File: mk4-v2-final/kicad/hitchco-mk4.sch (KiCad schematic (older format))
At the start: 24 parts, among them J1 Screw_Terminal_01x16, J10 Conn_02x03_Counter_Clockwise, J11 Conn_02x03_Counter_Clockwise, J12 Conn_02x03_Counter_Clockwise, J13 Screw_Terminal_01x16, J14 Conn_02x03_Counter_Clockwise, J15 Conn_02x03_Counter_Clockwise, J16 Conn_02x03_Counter_Clockwise, J17 Conn_02x03_Counter_Clockwise, J18 Conn_02x03_Counter_Clockwise, J19 Conn_02x03_Counter_Clockwise, J2 Conn_02x03_Counter_Clockwise, J20 Conn_02x03_Counter_Clockwise, J21 Conn_02x03_Counter_Clockwise, J22 Conn_02x03_Counter_Clockwise, J23 Conn_02x03_Counter_Clockwise, J24 Conn_02x03_Counter_Clockwise, J3 Conn_02x03_Counter_Clockwise, J4 Screw_Terminal_01x16, J5 Conn_02x03_Counter_Clockwise, J6 Conn_02x03_Counter_Clockwise, J7 Conn_02x03_Counter_Clockwise, J8 Screw_Terminal_01x16, J9 Conn_02x03_Counter_Clockwise

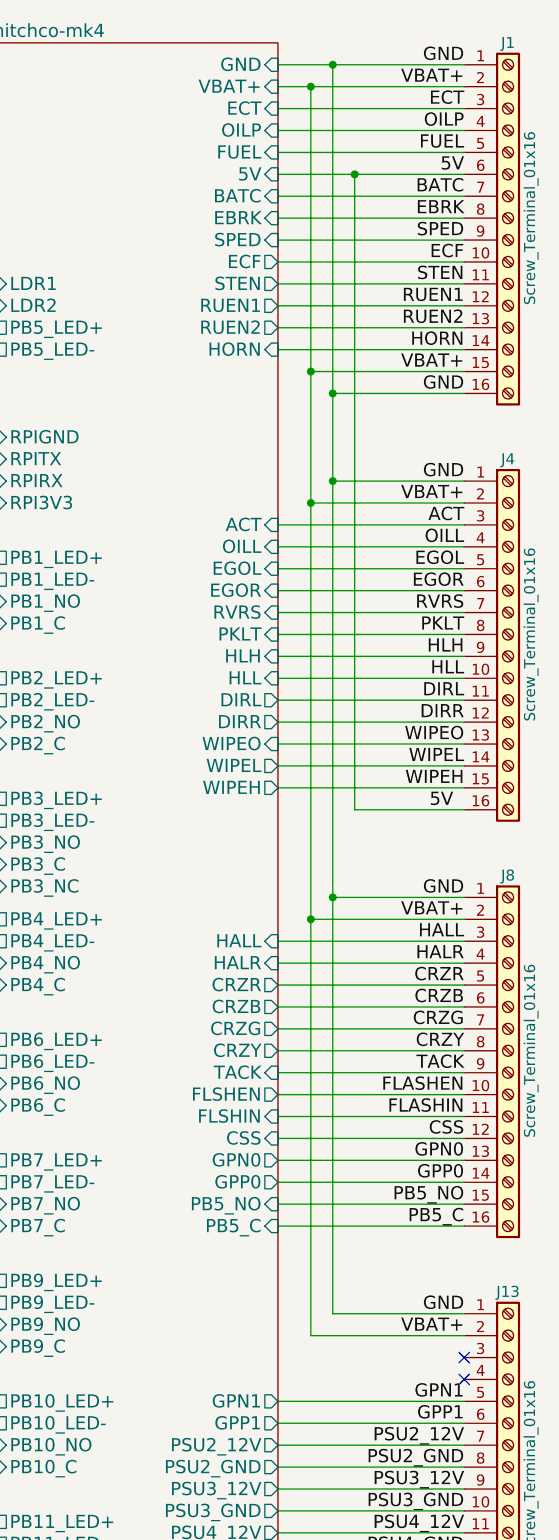
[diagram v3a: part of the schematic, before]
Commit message: all components on the board
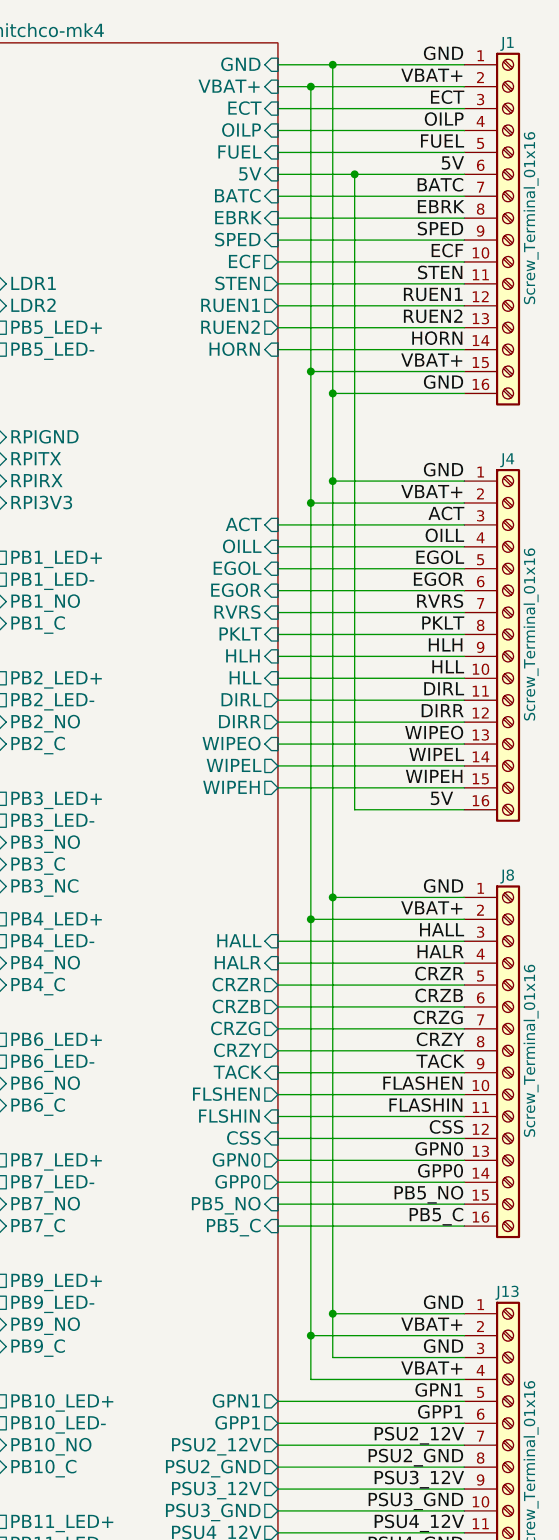
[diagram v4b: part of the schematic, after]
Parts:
- J1, J13, J4, J8: footprint TerminalBlocks_Phoenix:TerminalBlock_Phoenix_MKDS1.5-16pol -> TerminalBlock_Phoenix_45Deg_MKDS1:TerminalBlock_Phoenix_45Deg_MKDS1.5-16pol
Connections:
- net GND: now also J13.3 (Pin_3)
- net VBAT+: now also J13.4 (Pin_4)
- no-connect marks 40 -> 38
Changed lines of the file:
@@
 F 0 "J1" H 7700 2950 50  0000 C CNN
 F 1 "Screw_Terminal_01x16" V 7800 2150 50  0000 C CNN
-F 2 "TerminalBlocks_Phoenix:TerminalBlock_Phoenix_MKDS1.5-16pol" H 7700 2150 50  0001 C CNN
+F 2 "TerminalBlock_Phoenix_45Deg_MKDS1:TerminalBlock_Phoenix_45Deg_MKDS1.5-16pol" H 7700 2150 50  0001 C CNN
 F 3 "https://www.phoenixcontact.com/pxc-oc-itemdetail-pdf-web/eshop?lineItemType=LineItem&UID=1702972" H 7700 2150 50  0001 C CNN
 F 4 "277-13705-ND" H 7700 3050 50  0001 C CNN "digikey-pn"
@@
 F 0 "J4" H 7700 4850 50  0000 C CNN
 F 1 "Screw_Terminal_01x16" V 7800 4050 50  0000 C CNN
-F 2 "TerminalBlocks_Phoenix:TerminalBlock_Phoenix_MKDS1.5-16pol" H 7700 4050 50  0001 C CNN
+F 2 "TerminalBlock_Phoenix_45Deg_MKDS1:TerminalBlock_Phoenix_45Deg_MKDS1.5-16pol" H 7700 4050 50  0001 C CNN
 F 3 "https://www.phoenixcontact.com/pxc-oc-itemdetail-pdf-web/eshop?lineItemType=LineItem&UID=1702972" H 7700 4050 50  0001 C CNN
 F 4 "277-13705-ND" H 7700 4950 50  0001 C CNN "digikey-pn"
@@
 F 0 "J8" H 7700 6750 50  0000 C CNN
 F 1 "Screw_Terminal_01x16" V 7800 5950 50  0000 C CNN
-F 2 "TerminalBlocks_Phoenix:TerminalBlock_Phoenix_MKDS1.5-16pol" H 7700 5950 50  0001 C CNN
+F 2 "TerminalBlock_Phoenix_45Deg_MKDS1:TerminalBlock_Phoenix_45Deg_MKDS1.5-16pol" H 7700 5950 50  0001 C CNN
 F 3 "https://www.phoenixcontact.com/pxc-oc-itemdetail-pdf-web/eshop?lineItemType=LineItem&UID=1702972" H 7700 5950 50  0001 C CNN
 F 4 "277-13705-ND" H 7700 6850 50  0001 C CNN "digikey-pn"
@@
 F 0 "J13" H 7700 8650 50  0000 C CNN
 F 1 "Screw_Terminal_01x16" V 7800 7850 50  0000 C CNN
-F 2 "TerminalBlocks_Phoenix:TerminalBlock_Phoenix_MKDS1.5-16pol" H 7700 7850 50  0001 C CNN
+F 2 "TerminalBlock_Phoenix_45Deg_MKDS1:TerminalBlock_Phoenix_45Deg_MKDS1.5-16pol" H 7700 7850 50  0001 C CNN
 F 3 "https://www.phoenixcontact.com/pxc-oc-itemdetail-pdf-web/eshop?lineItemType=LineItem&UID=1702972" H 7700 7850 50  0001 C CNN
 F 4 "277-13705-ND" H 7700 8750 50  0001 C CNN "digikey-pn"
@@
 	6650 2750 7500 2750
 Wire Wire Line
-	6800 1550 6800 7250
+	6800 1550 6800 7450
 Wire Wire Line
 	6800 2850 7500 2850
@@
 	6650 4750 7500 4750
 Wire Wire Line
-	6900 1450 6900 7150
+	6900 1450 6900 7350
 Wire Wire Line
 	7000 4850 7500 4850
@@
 NoConn ~ 3900 3350
 NoConn ~ 3900 3450
-NoConn ~ 7500 7350
-NoConn ~ 7500 7450
+Wire Wire Line
+	6900 7350 7500 7350
+Connection ~ 6900 7150
+Wire Wire Line
+	6800 7450 7500 7450
+Connection ~ 6800 7250
+Text Label 7500 7450 2    60   ~ 0
+VBAT+
+Text Label 7500 7350 2    60   ~ 0
+GND
 $EndSCHEMATC
